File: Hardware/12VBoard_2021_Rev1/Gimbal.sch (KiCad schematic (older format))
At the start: 35 parts, among them Q6 CSD18537NQ5A, Q7 CSD18531Q5A, U12 LM5116, U13 INA198, U16 LM2576S-12/NOPB

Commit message: Checked H pins
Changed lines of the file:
@@
 EESchema Schematic File Version 4
-LIBS:12VBoard_2021_Rev1-cache
 EELAYER 30 0
 EELAYER END
@@
 HB
 Wire Wire Line
-	3700 1300 3650 1300
-Wire Wire Line
 	3700 900  3650 900
 Text GLabel 3700 900  2    50   Input ~ 0
@@
 $EndComp
 Wire Wire Line
-	1600 4150 1600 4100
-Wire Wire Line
 	1500 4100 1500 4150
 Wire Wire Line
@@
 Wire Wire Line
 	1525 3350 1625 3350
+Wire Wire Line
+	3650 1300 3700 1300
+Wire Wire Line
+	1600 4100 1600 4150
 $EndSCHEMATC

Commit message: Lunch Break
Routing thinzs
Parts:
- D23: footprint Diode_THT:D_DO-201AD_P15.24mm_Horizontal -> Diode_THT:D_DO-201AD_P5.08mm_Vertical_KathodeUp
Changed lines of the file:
@@
 F 0 "D23" V 8254 1605 50  0000 L CNN
 F 1 "D_Schottky" V 8345 1605 50  0000 L CNN
-F 2 "Diode_THT:D_DO-201AD_P15.24mm_Horizontal" H 8300 1525 50  0001 C CNN
+F 2 "Diode_THT:D_DO-201AD_P5.08mm_Vertical_KathodeUp" H 8300 1525 50  0001 C CNN
 F 3 "~" H 8300 1525 50  0001 C CNN
 	1    8300 1525
@@
 AR Path="/5F74F36B/5F8236F9/5FD3AF34" Ref="Q?"  Part="1"
 AR Path="/5F74F36B/5F971CD6/5FD3AF34" Ref="Q7"  Part="1"
+AR Path="/5FD3AF34" Ref="Q7"  Part="1"
 F 0 "Q7" V 1400 4225 50  0000 R CNN
 F 1 "CSD18531Q5A" V 1475 4650 50  0000 R CNN

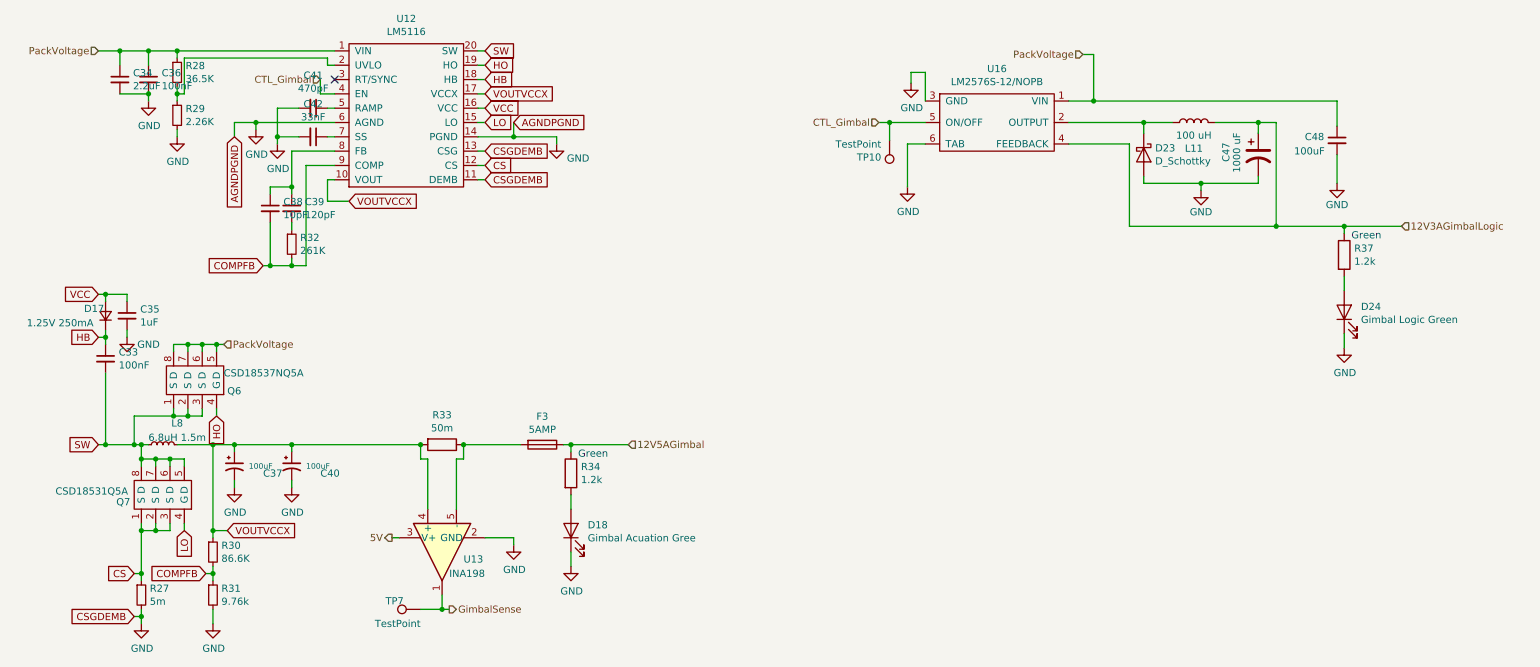
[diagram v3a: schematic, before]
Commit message: Changes!
Added the new correct connectors and redid all signal lines to the High Current side of the board. Also deleted all uncessacary components on the High current side that are no longer used.
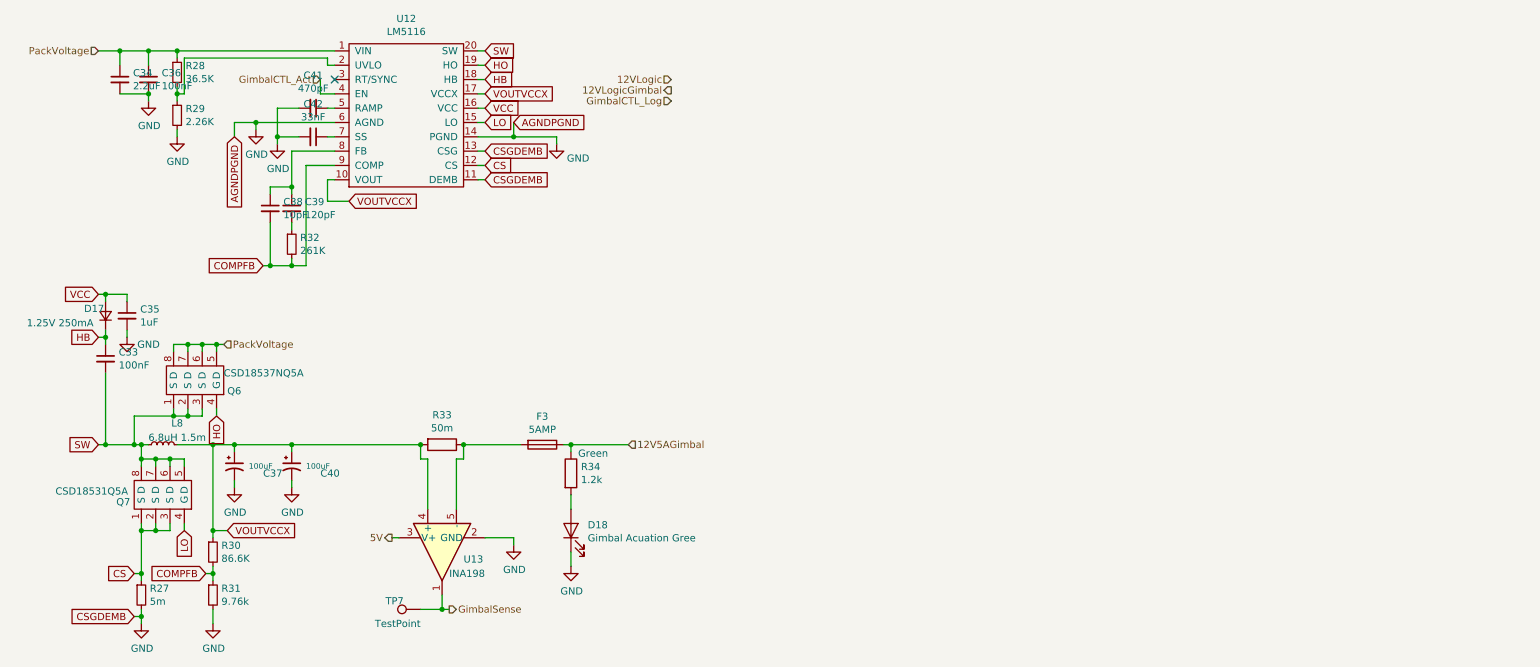
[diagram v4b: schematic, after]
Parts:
- removed C47: 1000 uF, Capacitor_THT:CP_Radial_D10.0mm_P5.00mm, symbol Device:CP1
- removed C48: 100uF, Capacitor_SMD:C_0603_1608Metric_Pad1.05x0.95mm_HandSolder, symbol Device:C_Small
- removed D23: D_Schottky, Diode_THT:D_DO-201AD_P5.08mm_Vertical_KathodeUp, symbol Device:D_Schottky
- removed D24: Gimbal Logic Green, Diode_SMD:D_0603_1608Metric_Pad1.05x0.95mm_HandSolder, symbol Device:LED
- removed L11: 100 uH, Inductor_SMD:L_0603_1608Metric_Pad1.05x0.95mm_HandSolder, symbol Device:L
- removed R37: 1.2k, Resistor_SMD:R_0603_1608Metric_Pad1.05x0.95mm_HandSolder, symbol Device:R
- removed TP10: TestPoint, TestPoint:TestPoint_Pad_2.5x2.5mm, symbol Connector:TestPoint
- removed U16: LM2576S-12/NOPB, MRDT_Devices:LM2576, symbol 12VBoard_2021_Rev1-rescue:LM2576D2TR4-MRDT_Devices
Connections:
- net CTL_Gimbal renamed GimbalCTL_Act

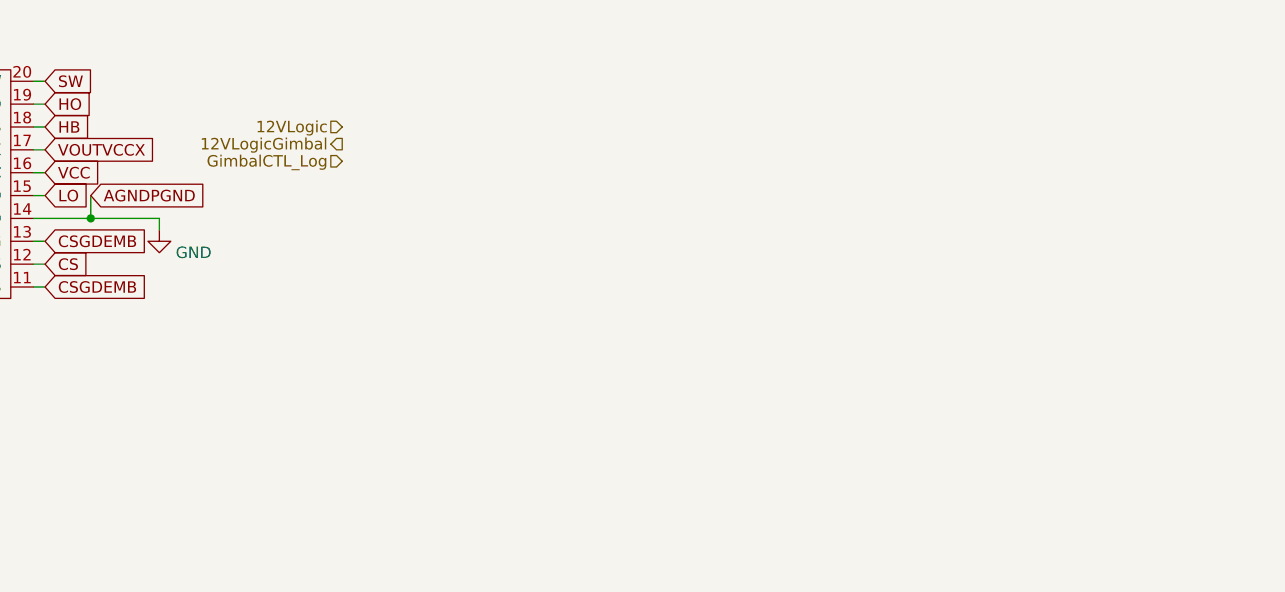
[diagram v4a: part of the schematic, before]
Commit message: Added Mosfet cicuitry to turn on/off logic power for high current side
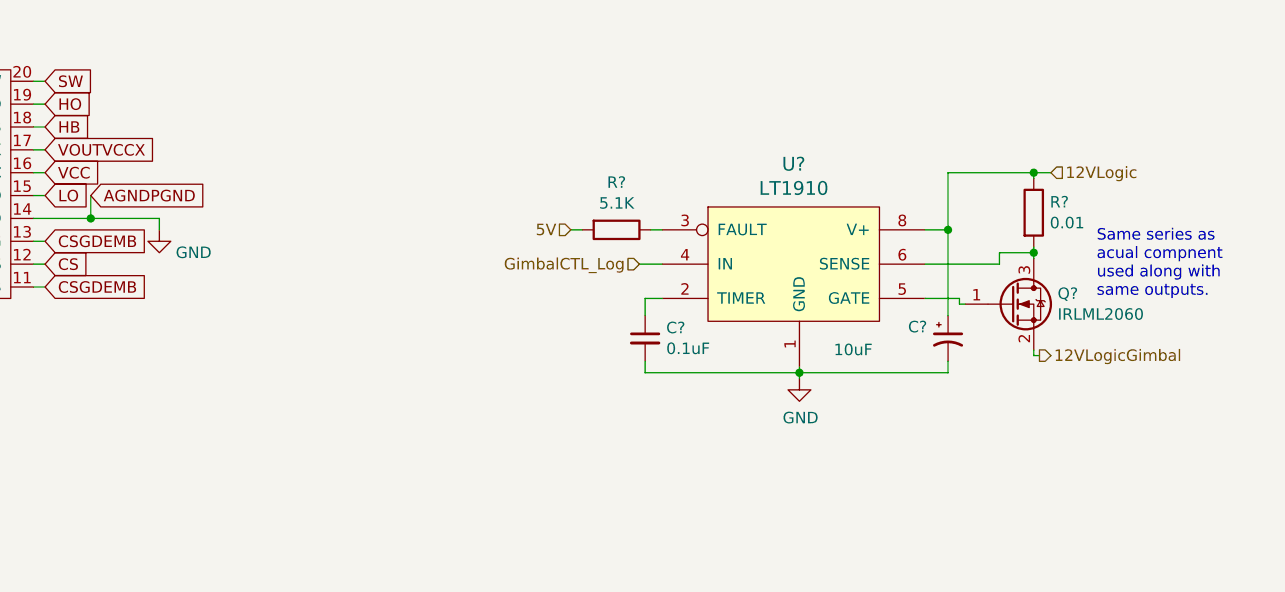
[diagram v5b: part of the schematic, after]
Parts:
- added C?: 0.1uF, symbol Device:C_Small
- added C?: 10uF, symbol Device:CP1_Small
- added Q?: IRLML2060, Package_TO_SOT_SMD:SOT-23, symbol Transistor_FET:IRLML2060
- added R?: 5.1K, symbol Device:R
- added R?: 0.01, symbol Device:R
- added U?: LT1910, symbol MRDT_ICs:LT1910
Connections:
- net 12VLogic: now also C?.1, R?.1, U?.8 (V+)
- net 12VLogicGimbal: now also Q?.2 (S)
- net 5V: now also R?.2
- net GND: now also C?.2, C?.2, U?.1 (GND)
- net GimbalCTL_Log: now also U?.4 (IN)
- new net: C?.1, U?.2 (TIMER)
- new net: R?.1, U?.3 (FAULT)
- new net: Q?.1 (G), U?.5 (GATE)
- new net: Q?.3 (D), R?.2, U?.6 (SENSE)
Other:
- note added: "Same series as \nacual compnent\nused along with\nsame outputs."
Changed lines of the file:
@@
 Wire Wire Line
 	1600 4100 1600 4150
-Text HLabel 5000 1000 0    50   Input ~ 0
+Text HLabel 8100 1200 2    50   Input ~ 0
 12VLogic
-Text HLabel 5000 1075 0    50   Output ~ 0
+Text HLabel 8050 2000 2    50   Output ~ 0
 12VLogicGimbal
-Text HLabel 5000 1150 0    50   Input ~ 0
+Text HLabel 6300 1600 0    50   Input ~ 0
 GimbalCTL_Log
+$Comp
+L MRDT_ICs:LT1910 U?
+U 1 1 5FB66D16
+P 6600 1850
+F 0 "U?" H 6975 2537 60  0000 C CNN
+F 1 "LT1910" H 6975 2431 60  0000 C CNN
+F 2 "" H 6600 1850 60  0001 C CNN
+F 3 "" H 6600 1850 60  0001 C CNN
+	1    6600 1850
+	1    0    0    -1
+$EndComp
+$Comp
+L Device:C_Small C?
+U 1 1 5FB6822F
+P 6325 1925
+F 0 "C?" H 6417 1971 50  0000 L CNN
+F 1 "0.1uF" H 6417 1880 50  0000 L CNN
+F 2 "" H 6325 1925 50  0001 C CNN
+F 3 "~" H 6325 1925 50  0001 C CNN
+	1    6325 1925
+	1    0    0    -1
+$EndComp
+$Comp
+L Device:CP1_Small C?
+U 1 1 5FB68B8A
+P 7650 1925
+F 0 "C?" H 7475 1975 50  0000 L CNN
+F 1 "10uF" H 7150 1875 50  0000 L CNN
+F 2 "" H 7650 1925 50  0001 C CNN
+F 3 "~" H 7650 1925 50  0001 C CNN
+	1    7650 1925
+	1    0    0    -1
+$EndComp
+$Comp
+L power:GND #PWR?
+U 1 1 5FB69837
+P 7000 2100
+F 0 "#PWR?" H 7000 1850 50  0001 C CNN
+F 1 "GND" H 7005 1927 50  0000 C CNN
+F 2 "" H 7000 2100 50  0001 C CNN
+F 3 "" H 7000 2100 50  0001 C CNN
+	1    7000 2100
+	1    0    0    -1
+$EndComp
+Wire Wire Line
+	7000 2050 7000 2075
+Wire Wire Line
+	7000 2100 7000 2075
+Connection ~ 7000 2075
+Wire Wire Line
+	7000 2075 6325 2075
+Wire Wire Line
+	6325 2075 6325 2025
+Wire Wire Line
+	7650 2025 7650 2075
+Wire Wire Line
+	7000 2075 7650 2075
+Wire Wire Line
+	7650 1825 7650 1450
+Wire Wire Line
+	7650 1450 7550 1450
+Wire Wire Line
+	6400 1750 6325 1750
+Wire Wire Line
+	6325 1750 6325 1825
+Wire Wire Line
+	6350 1450 6400 1450
+$Comp
+L Transistor_FET:IRLML2060 Q?
+U 1 1 5FBAA855
+P 7925 1775
+F 0 "Q?" H 8129 1821 50  0000 L CNN
+F 1 "IRLML2060" H 8129 1730 50  0000 L CNN
+F 2 "Package_TO_SOT_SMD:SOT-23" H 8125 1700 50  0001 L CIN
+F 3 "https://www.infineon.com/dgdl/irlml2060pbf.pdf?fileId=5546d462533600a401535664b7fb25ee" H 7925 1775 50  0001 L CNN
+	1    7925 1775
+	1    0    0    -1
+$EndComp
+Wire Wire Line
+	7550 1600 7875 1600
+Wire Wire Line
+	7875 1600 7875 1550
+Wire Wire Line
+	7875 1550 8025 1550
+Wire Wire Line
+	8025 1550 8025 1525
+Wire Wire Line
+	8025 1550 8025 1575
+Connection ~ 8025 1550
+Wire Wire Line
+	7650 1450 7650 1200
+Wire Wire Line
+	7650 1200 8025 1200
+Wire Wire Line
+	8025 1200 8025 1225
+Connection ~ 7650 1450
+Wire Wire Line
+	8050 2000 8025 2000
+Wire Wire Line
+	8025 2000 8025 1975
+Connection ~ 8025 1200
+Wire Wire Line
+	8025 1200 8100 1200
+Wire Wire Line
+	6300 1600 6400 1600
+Wire Wire Line
+	7725 1775 7700 1775
+Wire Wire Line
+	7700 1775 7700 1750
+Wire Wire Line
+	7700 1750 7550 1750
+Text Notes 8300 1750 0    50   ~ 0
+Same series as \nacual compnent\nused along with\nsame outputs.
+$Comp
+L Device:R R?
+U 1 1 5FBAFD11
+P 8025 1375
+F 0 "R?" H 8095 1421 50  0000 L CNN
+F 1 "0.01" H 8095 1330 50  0000 L CNN
+F 2 "" V 7955 1375 50  0001 C CNN
+F 3 "~" H 8025 1375 50  0001 C CNN
+	1    8025 1375
+	1    0    0    -1
+$EndComp
+$Comp
+L Device:R R?
+U 1 1 5FB98709
+P 6200 1450
+F 0 "R?" V 5993 1450 50  0000 C CNN
+F 1 "5.1K" V 6084 1450 50  0000 C CNN
+F 2 "" V 6130 1450 50  0001 C CNN
+F 3 "~" H 6200 1450 50  0001 C CNN
+	1    6200 1450
+	0    1    1    0
+$EndComp
+Text HLabel 6000 1450 0    50   Input ~ 0
+5V
+Wire Wire Line
+	6000 1450 6050 1450
 $EndSCHEMATC

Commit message: Redesigned low current ports schematic
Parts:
- gave numbers to parts that had none: 6
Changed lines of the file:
@@
 GimbalCTL_Log
 $Comp
-L MRDT_ICs:LT1910 U?
+L MRDT_ICs:LT1910 U3
 U 1 1 5FB66D16
 P 6600 1850
-F 0 "U?" H 6975 2537 60  0000 C CNN
+F 0 "U3" H 6975 2537 60  0000 C CNN
 F 1 "LT1910" H 6975 2431 60  0000 C CNN
 F 2 "" H 6600 1850 60  0001 C CNN
@@
 $EndComp
 $Comp
-L Device:C_Small C?
+L Device:C_Small C3
 U 1 1 5FB6822F
 P 6325 1925
-F 0 "C?" H 6417 1971 50  0000 L CNN
+F 0 "C3" H 6417 1971 50  0000 L CNN
 F 1 "0.1uF" H 6417 1880 50  0000 L CNN
 F 2 "" H 6325 1925 50  0001 C CNN
@@
 $EndComp
 $Comp
-L Device:CP1_Small C?
+L Device:CP1_Small C5
 U 1 1 5FB68B8A
 P 7650 1925
-F 0 "C?" H 7475 1975 50  0000 L CNN
+F 0 "C5" H 7475 1975 50  0000 L CNN
 F 1 "10uF" H 7150 1875 50  0000 L CNN
 F 2 "" H 7650 1925 50  0001 C CNN
@@
 $EndComp
 $Comp
-L power:GND #PWR?
+L power:GND #PWR04
 U 1 1 5FB69837
 P 7000 2100
-F 0 "#PWR?" H 7000 1850 50  0001 C CNN
+F 0 "#PWR04" H 7000 1850 50  0001 C CNN
 F 1 "GND" H 7005 1927 50  0000 C CNN
 F 2 "" H 7000 2100 50  0001 C CNN
@@
 	6350 1450 6400 1450
 $Comp
-L Transistor_FET:IRLML2060 Q?
+L Transistor_FET:IRLML2060 Q8
 U 1 1 5FBAA855
 P 7925 1775
-F 0 "Q?" H 8129 1821 50  0000 L CNN
+F 0 "Q8" H 8129 1821 50  0000 L CNN
 F 1 "IRLML2060" H 8129 1730 50  0000 L CNN
 F 2 "Package_TO_SOT_SMD:SOT-23" H 8125 1700 50  0001 L CIN
@@
 Same series as \nacual compnent\nused along with\nsame outputs.
 $Comp
-L Device:R R?
+L Device:R R7
 U 1 1 5FBAFD11
 P 8025 1375
-F 0 "R?" H 8095 1421 50  0000 L CNN
+F 0 "R7" H 8095 1421 50  0000 L CNN
 F 1 "0.01" H 8095 1330 50  0000 L CNN
 F 2 "" V 7955 1375 50  0001 C CNN
@@
 $EndComp
 $Comp
-L Device:R R?
+L Device:R R6
 U 1 1 5FB98709
 P 6200 1450
-F 0 "R?" V 5993 1450 50  0000 C CNN
+F 0 "R6" V 5993 1450 50  0000 C CNN
 F 1 "5.1K" V 6084 1450 50  0000 C CNN
 F 2 "" V 6130 1450 50  0001 C CNN

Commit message: Layed out logic power
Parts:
- C3: footprint (none) -> Capacitor_SMD:C_0603_1608Metric_Pad1.05x0.95mm_HandSolder
- C5: footprint (none) -> Capacitor_THT:CP_Radial_D5.0mm_P2.00mm
- R6, R7: footprint (none) -> Resistor_SMD:R_0603_1608Metric_Pad1.05x0.95mm_HandSolder
- U3: footprint (none) -> Package_SO:SOIC-8-N7_3.9x4.9mm_P1.27mm
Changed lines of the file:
@@
 F 0 "U3" H 6975 2537 60  0000 C CNN
 F 1 "LT1910" H 6975 2431 60  0000 C CNN
-F 2 "" H 6600 1850 60  0001 C CNN
+F 2 "Package_SO:SOIC-8-N7_3.9x4.9mm_P1.27mm" H 6600 1850 60  0001 C CNN
 F 3 "" H 6600 1850 60  0001 C CNN
 	1    6600 1850
@@
 F 0 "C3" H 6417 1971 50  0000 L CNN
 F 1 "0.1uF" H 6417 1880 50  0000 L CNN
-F 2 "" H 6325 1925 50  0001 C CNN
+F 2 "Capacitor_SMD:C_0603_1608Metric_Pad1.05x0.95mm_HandSolder" H 6325 1925 50  0001 C CNN
 F 3 "~" H 6325 1925 50  0001 C CNN
 	1    6325 1925
@@
 F 0 "C5" H 7475 1975 50  0000 L CNN
 F 1 "10uF" H 7150 1875 50  0000 L CNN
-F 2 "" H 7650 1925 50  0001 C CNN
+F 2 "Capacitor_THT:CP_Radial_D5.0mm_P2.00mm" H 7650 1925 50  0001 C CNN
 F 3 "~" H 7650 1925 50  0001 C CNN
 	1    7650 1925
@@
 F 0 "R7" H 8095 1421 50  0000 L CNN
 F 1 "0.01" H 8095 1330 50  0000 L CNN
-F 2 "" V 7955 1375 50  0001 C CNN
+F 2 "Resistor_SMD:R_0603_1608Metric_Pad1.05x0.95mm_HandSolder" V 7955 1375 50  0001 C CNN
 F 3 "~" H 8025 1375 50  0001 C CNN
 	1    8025 1375
@@
 F 0 "R6" V 5993 1450 50  0000 C CNN
 F 1 "5.1K" V 6084 1450 50  0000 C CNN
-F 2 "" V 6130 1450 50  0001 C CNN
+F 2 "Resistor_SMD:R_0603_1608Metric_Pad1.05x0.95mm_HandSolder" V 6130 1450 50  0001 C CNN
 F 3 "~" H 6200 1450 50  0001 C CNN
 	1    6200 1450

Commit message: Started layout of bucks
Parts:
- L8: footprint Inductor_SMD:L_0603_1608Metric_Pad1.05x0.95mm_HandSolder -> MRDT_12VoltBoard:IND_SER2915L-682KL
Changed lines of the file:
@@
 F 0 "L8" V 1600 3450 50  0000 C CNN
 F 1 "6.8uH 1.5m" V 1500 3450 50  0000 C CNN
-F 2 "Inductor_SMD:L_0603_1608Metric_Pad1.05x0.95mm_HandSolder" H 1450 3550 50  0001 C CNN
+F 2 "MRDT_12VoltBoard:IND_SER2915L-682KL" H 1450 3550 50  0001 C CNN
 F 3 "~" H 1450 3550 50  0001 C CNN
 	1    1450 3550
